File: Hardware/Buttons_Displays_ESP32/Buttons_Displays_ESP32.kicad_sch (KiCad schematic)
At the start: 24 parts, among them J1 1778612, J2 1778612, J3 1778612, J4 1778612, J5 i2c, J6 USB_C_Receptacle_USB2.0_16P, SW1 SW_Push, SW2 SW_Push, U1 ESP32-S3-WROOM-1, U2 USBLC6-2P6

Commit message: pcb outlines
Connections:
- no-connect marks 10 -> 11
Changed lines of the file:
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@@
+	)
+	(no_connect
+		(at 88.9 72.39)
 	)
 	(no_connect
@@
 		(on_board yes)
 		(dnp no)
-		(fields_autoplaced yes)
 		(property "Reference" "U1"
 			(at 106.3341 44.45 0)

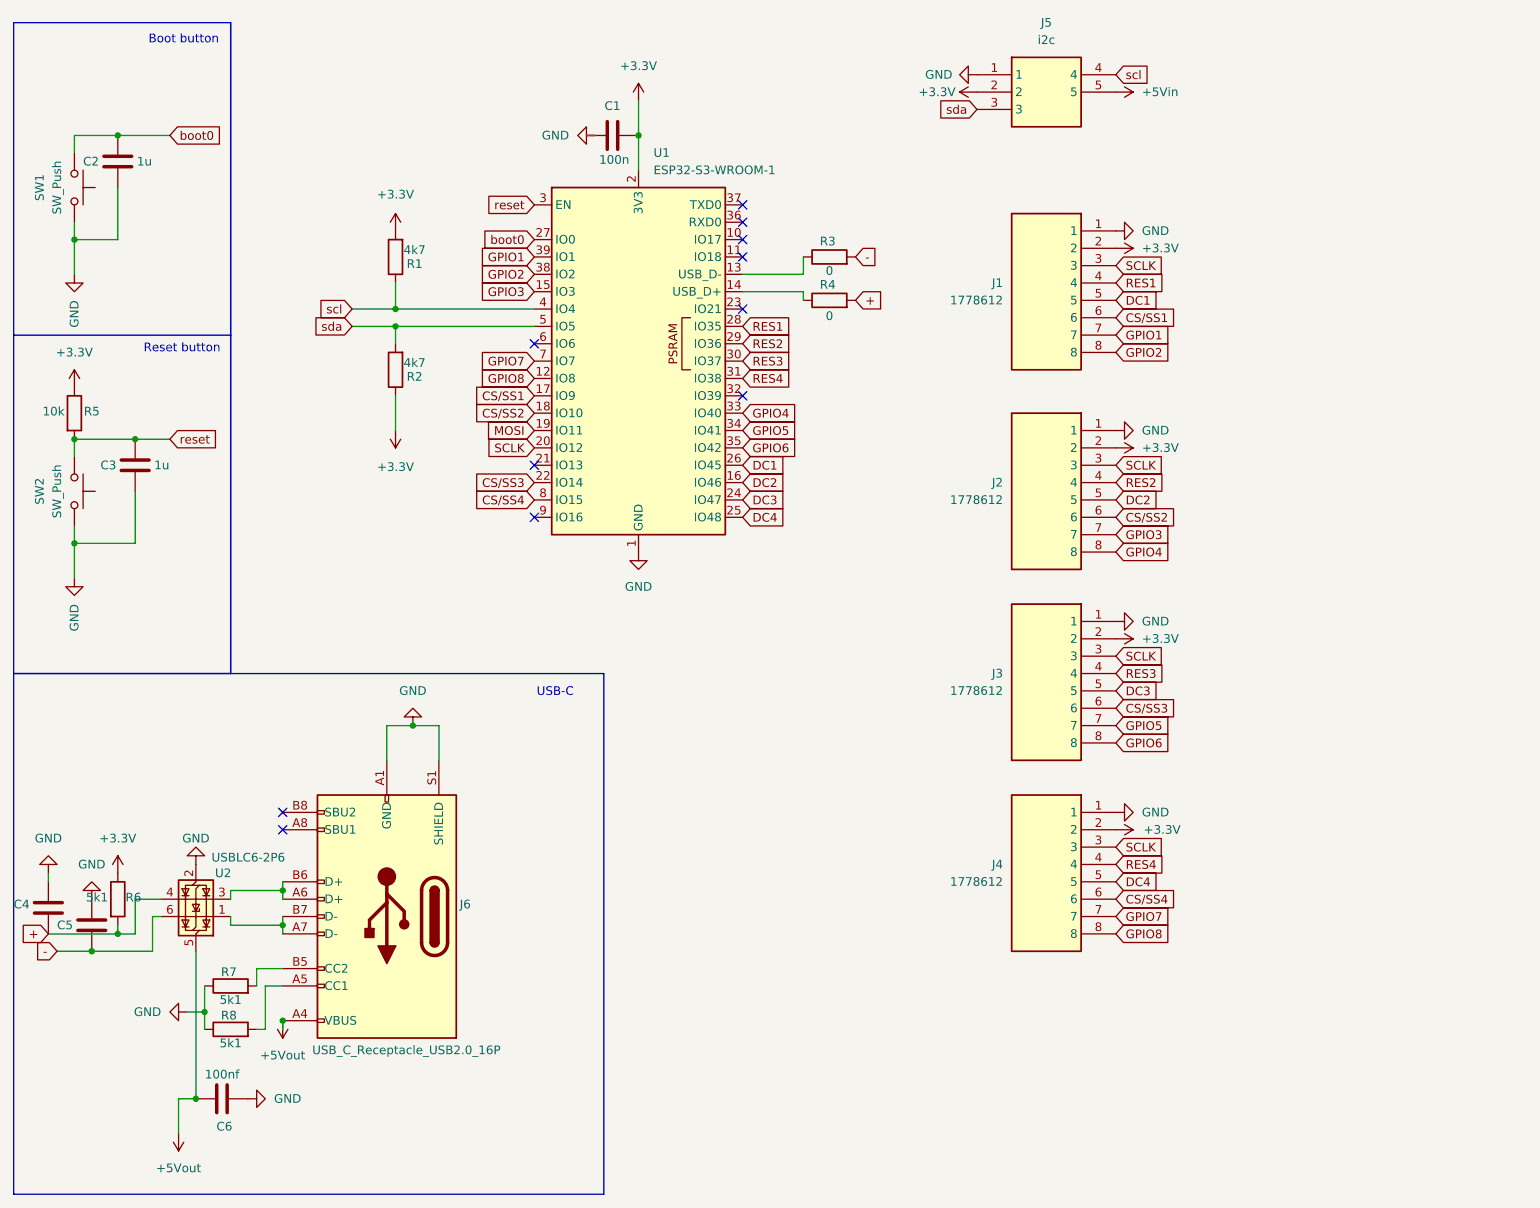
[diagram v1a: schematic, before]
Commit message: Kut ipo ;)
IO pin voor tril motor toegevoegd
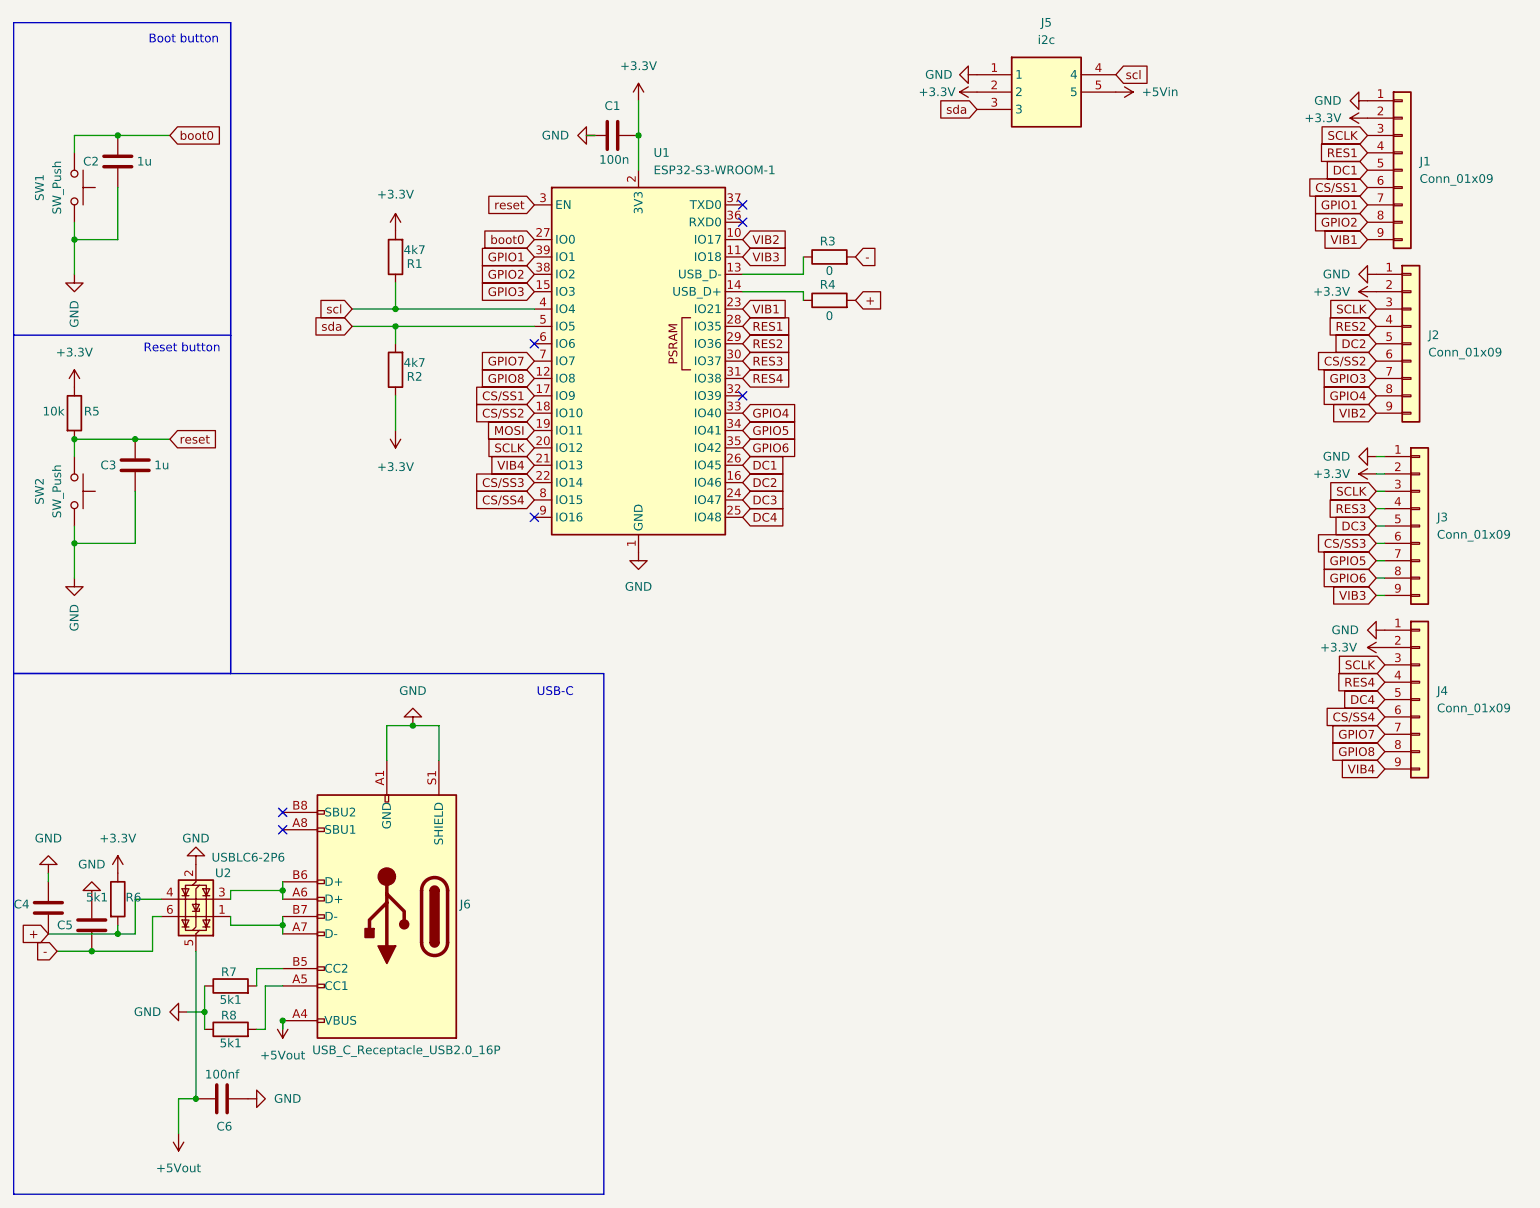
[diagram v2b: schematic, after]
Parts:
- removed J1, J2, J3, J4: 1778612, 1778612, symbol Connector_pt_phoenix:1778612
- added J1, J2, J3, J4: Conn_01x09, Connector_JST:JST_XH_B9B-XH-A_1x09_P2.50mm_Vertical, symbol Connector_Generic:Conn_01x09
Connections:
- net +3.3V: now also J1.2 (Pin_2), J2.2 (Pin_2), J3.2 (Pin_2), J4.2 (Pin_2)
- net CS/SS1: now also J1.6 (Pin_6)
- net CS/SS2: now also J2.6 (Pin_6)
- net CS/SS3: now also J3.6 (Pin_6)
- net CS/SS4: now also J4.6 (Pin_6)
- net DC1: now also J1.5 (Pin_5)
- net DC2: now also J2.5 (Pin_5)
- net DC3: now also J3.5 (Pin_5)
- net DC4: now also J4.5 (Pin_5)
- net GND: now also J1.1 (Pin_1), J2.1 (Pin_1), J3.1 (Pin_1), J4.1 (Pin_1)
- net GPIO1: now also J1.7 (Pin_7)
- net GPIO2: now also J1.8 (Pin_8)
- net GPIO3: now also J2.7 (Pin_7)
- net GPIO4: now also J2.8 (Pin_8)
- net GPIO5: now also J3.7 (Pin_7)
- net GPIO6: now also J3.8 (Pin_8)
- net GPIO7: now also J4.7 (Pin_7)
- net GPIO8: now also J4.8 (Pin_8)
- net RES1: now also J1.4 (Pin_4)
- net RES2: now also J2.4 (Pin_4)
- net RES3: now also J3.4 (Pin_4)
- net RES4: now also J4.4 (Pin_4)
- net SCLK: now also J1.3 (Pin_3), J2.3 (Pin_3), J3.3 (Pin_3), J4.3 (Pin_3)
- net VIB2: now reaches U1.10 (IO17)
- net VIB2: now also J2.9 (Pin_9)
- net VIB3: now reaches U1.11 (IO18)
- net VIB3: now also J3.9 (Pin_9)
- net VIB4: now reaches U1.21 (IO13)
- net VIB4: now also J4.9 (Pin_9)
- net VIB1: now reaches U1.23 (IO21)
- net VIB1: now also J1.9 (Pin_9)
- no-connect marks 11 -> 7

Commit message: laatste aanpassingen
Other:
- moved on the sheet: J1, J2, J3, J4
